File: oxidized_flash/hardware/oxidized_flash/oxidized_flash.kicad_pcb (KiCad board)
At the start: 2 copper layers, 61 x 21.6 mm, 20 parts, among them J1 USB_A, J2 Conn_ARM_JTAG_SWD_10, U1 LM1117-3.3, U2 ATSAMD51G18A-MU, U3 MT25QL

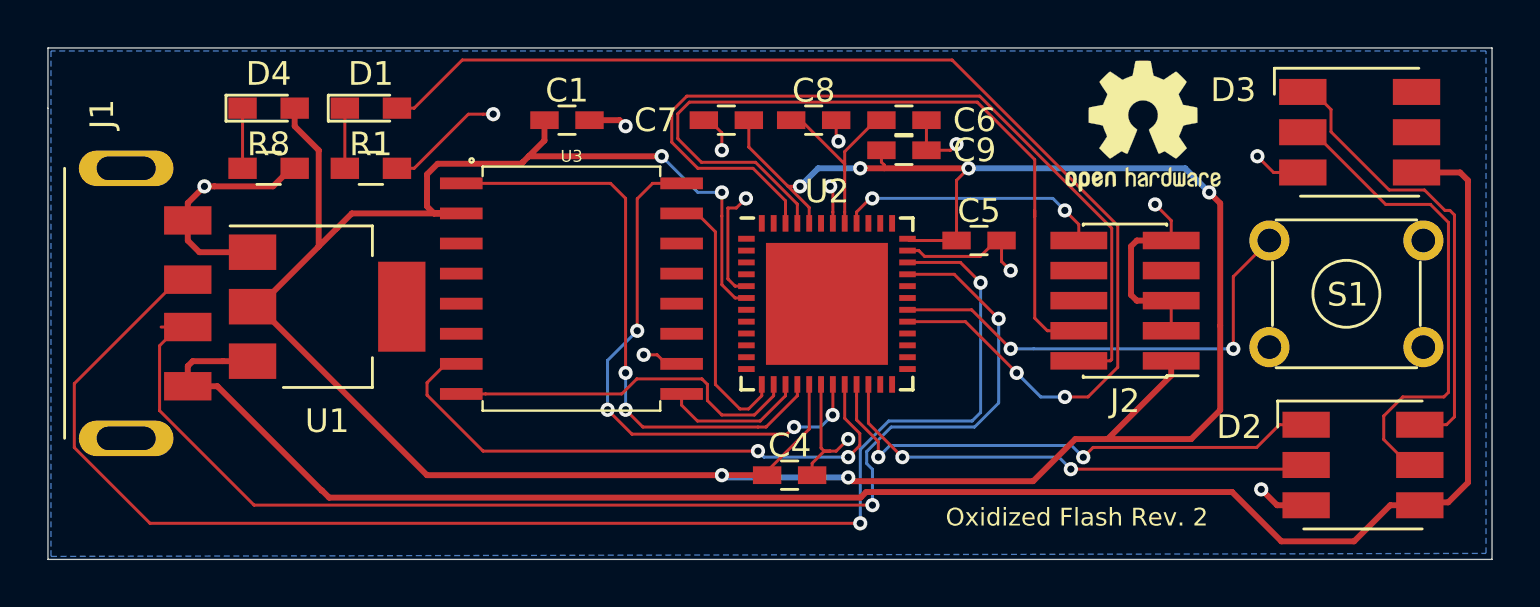
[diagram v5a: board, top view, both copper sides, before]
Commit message: Connect reset lines to the flash memory
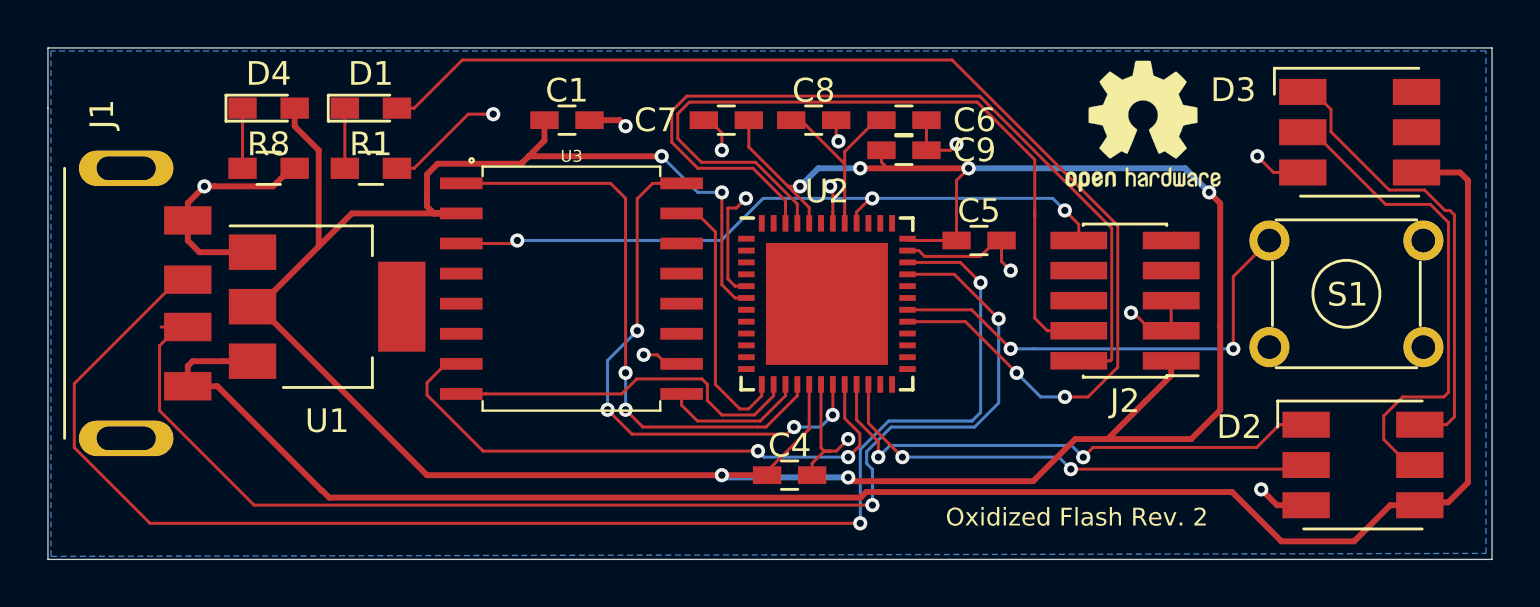
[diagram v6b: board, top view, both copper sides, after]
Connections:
- J2 pad 9: GND -> Net-(J2-Pad9)
- U3 pad 3: Net-(U3-Pad3) -> /SWD_RST
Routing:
- net /SWD_RST: track 11.2 -> 29.4 mm, vias 2 -> 3
- net GND: track 55.6 -> 50.2 mm
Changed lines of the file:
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@@
     (thickness 1.6)
     (drawings 6)
-    (tracks 384)
+    (tracks 386)
     (zones 0)
     (modules 20)
@@
   )
   (setup
-    (last_trace_width 0.25)
+    (last_trace_width 0.127)
     (user_trace_width 0.127)
     (trace_clearance 0.127)
@@
   (net 53 "Net-(U2-Pad1)")
   (net 54 "Net-(U2-Pad43)")
-  (net 55 "Net-(U3-Pad3)")
+  (net 55 "Net-(J2-Pad9)")
   (net_class Default "This is the default net class."
     (clearance 0.127)
@@
     (add_net "Net-(J2-Pad7)")
     (add_net "Net-(J2-Pad8)")
+    (add_net "Net-(J2-Pad9)")
     (add_net "Net-(S1-Pad2)")
     (add_net "Net-(S1-Pad4)")
@@
     (add_net "Net-(U2-Pad8)")
     (add_net "Net-(U2-Pad9)")
-    (add_net "Net-(U3-Pad3)")
   )
   (net_class BGA ""
@@
       (net 40 "Net-(U2-Pad16)"))
     (pad 3 smd rect (at -1.905 4.65 270) (size 0.5 1.8) (layers F.Cu F.Paste F.Mask)
-      (net 55 "Net-(U3-Pad3)"))
+      (net 2 /SWD_RST))
     (pad 2 smd rect (at -3.175 4.65 270) (size 0.5 1.8) (layers F.Cu F.Paste F.Mask)
       (net 3 +3V3))
@@
       (net 2 /SWD_RST))
     (pad 9 smd rect (at -1.95 2.54 180) (size 2.4 0.74) (layers F.Cu F.Paste F.Mask)
-      (net 1 GND))
+      (net 55 "Net-(J2-Pad9)"))
     (pad 8 smd rect (at 1.95 1.27 180) (size 2.4 0.74) (layers F.Cu F.Paste F.Mask)
       (net 17 "Net-(J2-Pad8)"))
@@
   (segment (start 56.76425 37.20625) (end 56.896 37.338) (width 0.127) (layer F.Cu) (net 1))
   (segment (start 56.76425 34.52375) (end 56.76425 37.20625) (width 0.127) (layer F.Cu) (net 1))
-  (segment (start 71.546 28.448) (end 71.546 27.604) (width 0.127) (layer F.Cu) (net 1))
-  (via (at 70.866 26.924) (size 0.6) (drill 0.3) (layers F.Cu B.Cu) (net 1))
-  (segment (start 71.546 27.604) (end 70.866 26.924) (width 0.127) (layer F.Cu) (net 1))
   (segment (start 71.546 32.258) (end 71.546 30.988) (width 0.127) (layer F.Cu) (net 1))
   (segment (start 71.546 30.988) (end 70.716 30.988) (width 0.127) (layer F.Cu) (net 1))
@@
   (segment (start 77.242 39.624) (end 76.019044 39.624) (width 0.25) (layer F.Cu) (net 1))
   (segment (start 76.019044 39.624) (end 75.347522 38.952478) (width 0.25) (layer F.Cu) (net 1))
-  (segment (start 70.096 28.448) (end 71.546 28.448) (width 0.25) (layer F.Cu) (net 1))
-  (segment (start 69.85 30.742) (end 69.85 28.694) (width 0.25) (layer F.Cu) (net 1))
-  (segment (start 69.85 28.694) (end 70.096 28.448) (width 0.25) (layer F.Cu) (net 1))
-  (segment (start 70.096 30.988) (end 69.85 30.742) (width 0.25) (layer F.Cu) (net 1))
-  (segment (start 71.546 30.988) (end 70.096 30.988) (width 0.25) (layer F.Cu) (net 1))
   (segment (start 30.032 28.45) (end 30.032 27.6) (width 0.25) (layer F.Cu) (net 1))
   (segment (start 30.524 28.942) (end 30.032 28.45) (width 0.25) (layer F.Cu) (net 1))
@@
   (segment (start 64.384 28.448) (end 64.384 29.332) (width 0.127) (layer F.Cu) (net 1))
   (segment (start 64.384 29.332) (end 64.77 29.718) (width 0.127) (layer F.Cu) (net 1))
+  (via (at 69.85 31.496) (size 0.6) (drill 0.3) (layers F.Cu B.Cu) (net 1))
+  (segment (start 69.954 31.496) (end 69.85 31.496) (width 0.127) (layer F.Cu) (net 1))
+  (segment (start 71.546 32.258) (end 70.716 32.258) (width 0.127) (layer F.Cu) (net 1))
+  (segment (start 70.716 32.258) (end 69.954 31.496) (width 0.127) (layer F.Cu) (net 1))
   (segment (start 58.841 26.67) (end 58.928 26.67) (width 0.127) (layer F.Cu) (net 2))
   (segment (start 58.26425 27.72375) (end 58.26425 27.24675) (width 0.127) (layer F.Cu) (net 2))
@@
   (segment (start 67.646 27.768) (end 67.646 28.448) (width 0.127) (layer F.Cu) (net 2))
   (segment (start 67.056 27.178) (end 67.646 27.768) (width 0.127) (layer F.Cu) (net 2))
+  (segment (start 41.578 28.575) (end 43.815 28.575) (width 0.127) (layer F.Cu) (net 2))
+  (via (at 43.942 28.448) (size 0.6) (drill 0.3) (layers F.Cu B.Cu) (net 2))
+  (segment (start 43.815 28.575) (end 43.942 28.448) (width 0.127) (layer F.Cu) (net 2))
+  (segment (start 52.541942 28.448) (end 54.319942 26.67) (width 0.127) (layer B.Cu) (net 2))
+  (segment (start 43.942 28.448) (end 52.541942 28.448) (width 0.127) (layer B.Cu) (net 2))
+  (segment (start 54.319942 26.67) (end 58.928 26.67) (width 0.127) (layer B.Cu) (net 2))
   (segment (start 56.26425 27.72375) (end 56.26425 27.05325) (width 0.127) (layer F.Cu) (net 3))
   (segment (start 71.546 33.528) (end 72.376 33.528) (width 0.25) (layer F.Cu) (net 3))
@@
   (segment (start 57.76425 24.69275) (end 59.089 23.368) (width 0.127) (layer F.Cu) (net 4))
   (segment (start 57.76425 25.21925) (end 57.76425 24.69275) (width 0.127) (layer F.Cu) (net 4))
+  (segment (start 65.024 34.036) (end 62.86175 31.87375) (width 0.127) (layer F.Cu) (net 5))
+  (segment (start 62.86175 31.87375) (end 60.41425 31.87375) (width 0.127) (layer F.Cu) (net 5))
+  (segment (start 66.04 35.052) (end 65.024 34.036) (width 0.127) (layer B.Cu) (net 5))
+  (segment (start 67.056 35.052) (end 66.04 35.052) (width 0.127) (layer B.Cu) (net 5))
+  (via (at 65.024 34.036) (size 0.6) (drill 0.3) (layers F.Cu B.Cu) (net 5))
+  (via (at 67.056 35.052) (size 0.6) (drill 0.3) (layers F.Cu B.Cu) (net 5))
+  (segment (start 68.034902 35.052) (end 67.056 35.052) (width 0.127) (layer F.Cu) (net 5))
+  (segment (start 69.290511 33.796391) (end 68.034902 35.052) (width 0.127) (layer F.Cu) (net 5))
+  (segment (start 39.589 22.86) (end 41.621 20.828) (width 0.127) (layer F.Cu) (net 5))
+  (segment (start 62.298126 20.828) (end 69.290511 27.820385) (width 0.127) (layer F.Cu) (net 5))
+  (segment (start 69.290511 27.820385) (end 69.290511 33.796391) (width 0.127) (layer F.Cu) (net 5))
+  (segment (start 38.862 22.86) (end 39.589 22.86) (width 0.127) (layer F.Cu) (net 5))
+  (segment (start 41.621 20.828) (end 62.298126 20.828) (width 0.127) (layer F.Cu) (net 5))
+  (segment (start 36.662 25.4) (end 36.662 22.86) (width 0.127) (layer F.Cu) (net 6))
   (segment (start 59.182 37.592) (end 59.182 36.935224) (width 0.127) (layer F.Cu) (net 7))
   (segment (start 59.182 36.935224) (end 58.26425 36.017474) (width 0.127) (layer F.Cu) (net 7))
@@
   (segment (start 82.163999 39.502001) (end 82.042 39.624) (width 0.25) (layer F.Cu) (net 10))
   (segment (start 83.239601 39.502001) (end 82.163999 39.502001) (width 0.25) (layer F.Cu) (net 10))
-  (via (at 67.31 38.1) (size 0.6) (drill 0.3) (layers F.Cu B.Cu) (net 11))
-  (via (at 60.198 37.592) (size 0.6) (drill 0.3) (layers F.Cu B.Cu) (net 11))
-  (segment (start 67.31 38.1) (end 66.802 37.592) (width 0.127) (layer B.Cu) (net 11))
-  (segment (start 66.802 37.592) (end 60.198 37.592) (width 0.127) (layer B.Cu) (net 11))
-  (segment (start 58.76425 36.15825) (end 58.76425 34.52375) (width 0.127) (layer F.Cu) (net 11))
-  (segment (start 60.198 37.592) (end 58.76425 36.15825) (width 0.127) (layer F.Cu) (net 11))
-  (segment (start 77.066 38.1) (end 77.242 37.924) (width 0.127) (layer F.Cu) (net 11))
-  (segment (start 67.31 38.1) (end 77.066 38.1) (width 0.127) (layer F.Cu) (net 11))
-  (segment (start 65.024 34.036) (end 62.86175 31.87375) (width 0.127) (layer F.Cu) (net 5))
-  (segment (start 62.86175 31.87375) (end 60.41425 31.87375) (width 0.127) (layer F.Cu) (net 5))
-  (segment (start 66.04 35.052) (end 65.024 34.036) (width 0.127) (layer B.Cu) (net 5))
-  (segment (start 67.056 35.052) (end 66.04 35.052) (width 0.127) (layer B.Cu) (net 5))
-  (via (at 65.024 34.036) (size 0.6) (drill 0.3) (layers F.Cu B.Cu) (net 5))
-  (via (at 67.056 35.052) (size 0.6) (drill 0.3) (layers F.Cu B.Cu) (net 5))
-  (segment (start 68.034902 35.052) (end 67.056 35.052) (width 0.127) (layer F.Cu) (net 5))
-  (segment (start 69.290511 33.796391) (end 68.034902 35.052) (width 0.127) (layer F.Cu) (net 5))
-  (segment (start 39.589 22.86) (end 41.621 20.828) (width 0.127) (layer F.Cu) (net 5))
-  (segment (start 62.298126 20.828) (end 69.290511 27.820385) (width 0.127) (layer F.Cu) (net 5))
-  (segment (start 69.290511 27.820385) (end 69.290511 33.796391) (width 0.127) (layer F.Cu) (net 5))
-  (segment (start 38.862 22.86) (end 39.589 22.86) (width 0.127) (layer F.Cu) (net 5))
-  (segment (start 41.621 20.828) (end 62.298126 20.828) (width 0.127) (layer F.Cu) (net 5))
-  (segment (start 36.662 25.4) (end 36.662 22.86) (width 0.127) (layer F.Cu) (net 6))
   (segment (start 80.792 39.624) (end 82.042 39.624) (width 0.25) (layer F.Cu) (net 10))
   (segment (start 74.117931 39.065931) (end 76.2 41.148) (width 0.25) (layer F.Cu) (net 10))
@@
   (segment (start 35.698 39) (end 36.000422 39.302422) (width 0.25) (layer F.Cu) (net 10))
   (segment (start 36.000422 39.302422) (end 58.432616 39.302422) (width 0.25) (layer F.Cu) (net 10))
+  (via (at 67.31 38.1) (size 0.6) (drill 0.3) (layers F.Cu B.Cu) (net 11))
+  (via (at 60.198 37.592) (size 0.6) (drill 0.3) (layers F.Cu B.Cu) (net 11))
+  (segment (start 67.31 38.1) (end 66.802 37.592) (width 0.127) (layer B.Cu) (net 11))
+  (segment (start 66.802 37.592) (end 60.198 37.592) (width 0.127) (layer B.Cu) (net 11))
+  (segment (start 58.76425 36.15825) (end 58.76425 34.52375) (width 0.127) (layer F.Cu) (net 11))
+  (segment (start 60.198 37.592) (end 58.76425 36.15825) (width 0.127) (layer F.Cu) (net 11))
+  (segment (start 77.066 38.1) (end 77.242 37.924) (width 0.127) (layer F.Cu) (net 11))
+  (segment (start 67.31 38.1) (end 77.066 38.1) (width 0.127) (layer F.Cu) (net 11))
   (segment (start 32.344 25.4) (end 32.344 22.86) (width 0.127) (layer F.Cu) (net 14))
   (via (at 64.262 31.75) (size 0.6) (drill 0.3) (layers F.Cu B.Cu) (net 15))
